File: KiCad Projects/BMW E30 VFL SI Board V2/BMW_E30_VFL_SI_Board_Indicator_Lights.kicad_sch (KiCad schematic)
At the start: 14 parts, among them J1 Conn_01x13_Pin, Q5 BC337-25, Q6 BC337-25, Q7 BC337-25

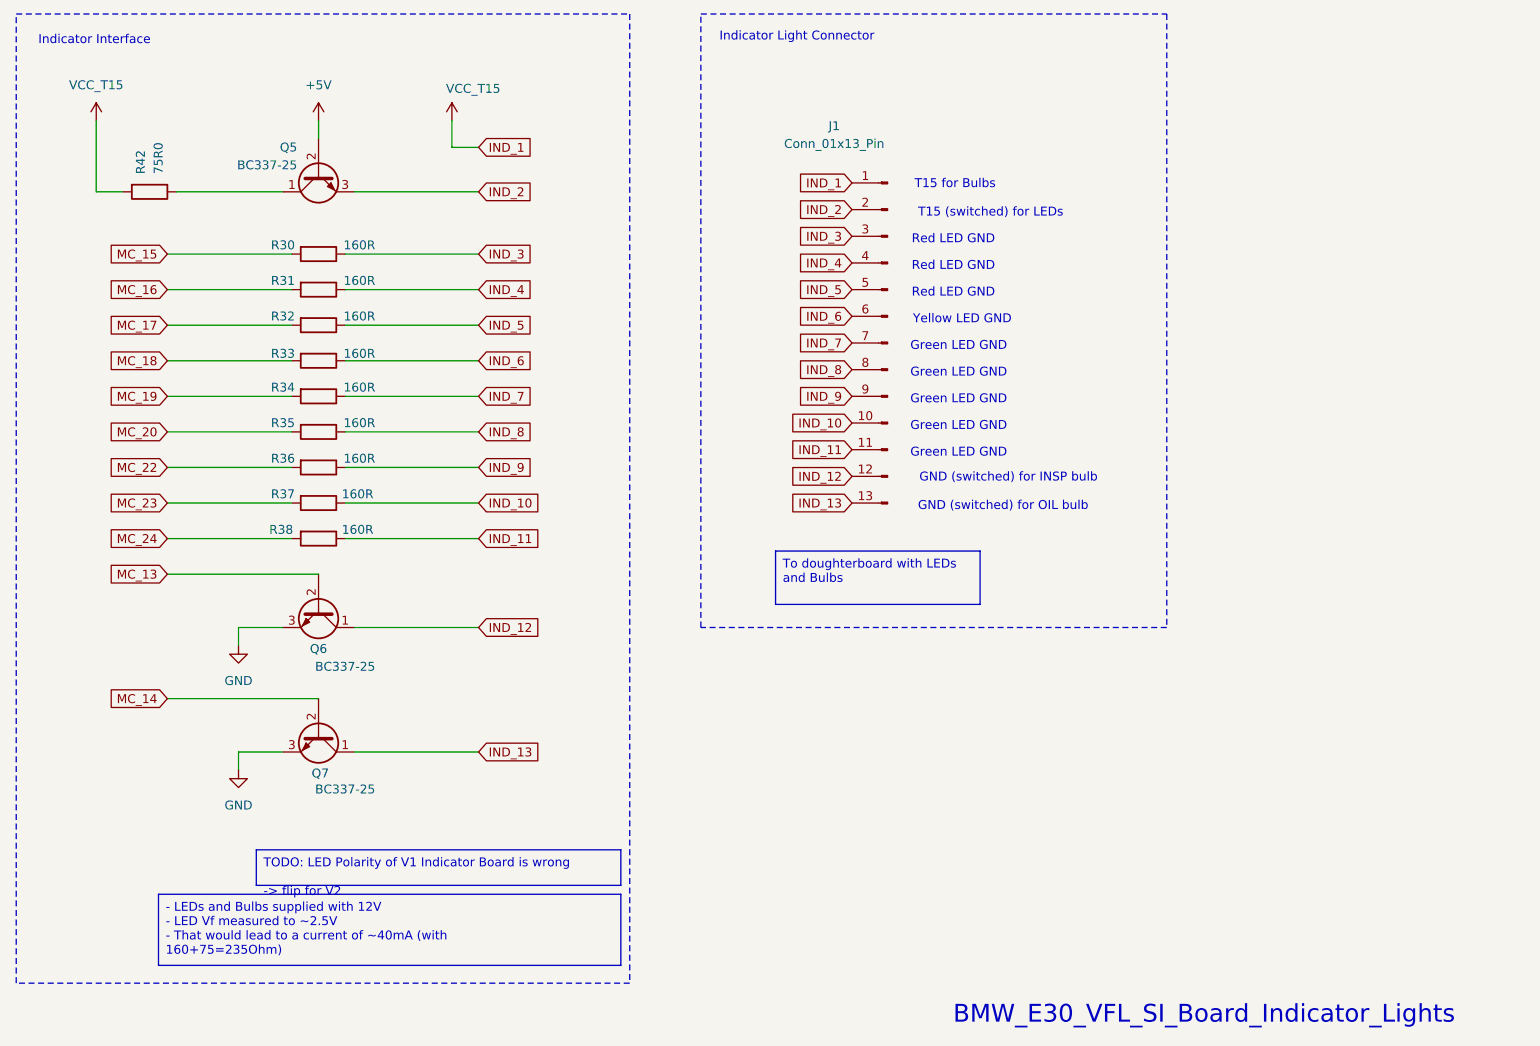
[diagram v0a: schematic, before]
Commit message: V2 Board Updates
Added in extra resistors, cap, and diode that were added to a  particular version of the SI board from the USDM on the comparator circuit. Updated the schematic diagram of the comparator circuit to improve readability. Updated the clock frequency measured with a scope. Made a few minor layout improvements including moving the "JP" connections inwards as not to interfere with the plastic housing for the PCB in the cluster and other minor layout errors such as swapped reference designators. Updated info on where the +5V regulator gets its source voltage from. These updates are reflected in schematic version V2.1 as denoted in the title box (not in the title of the schematic file).
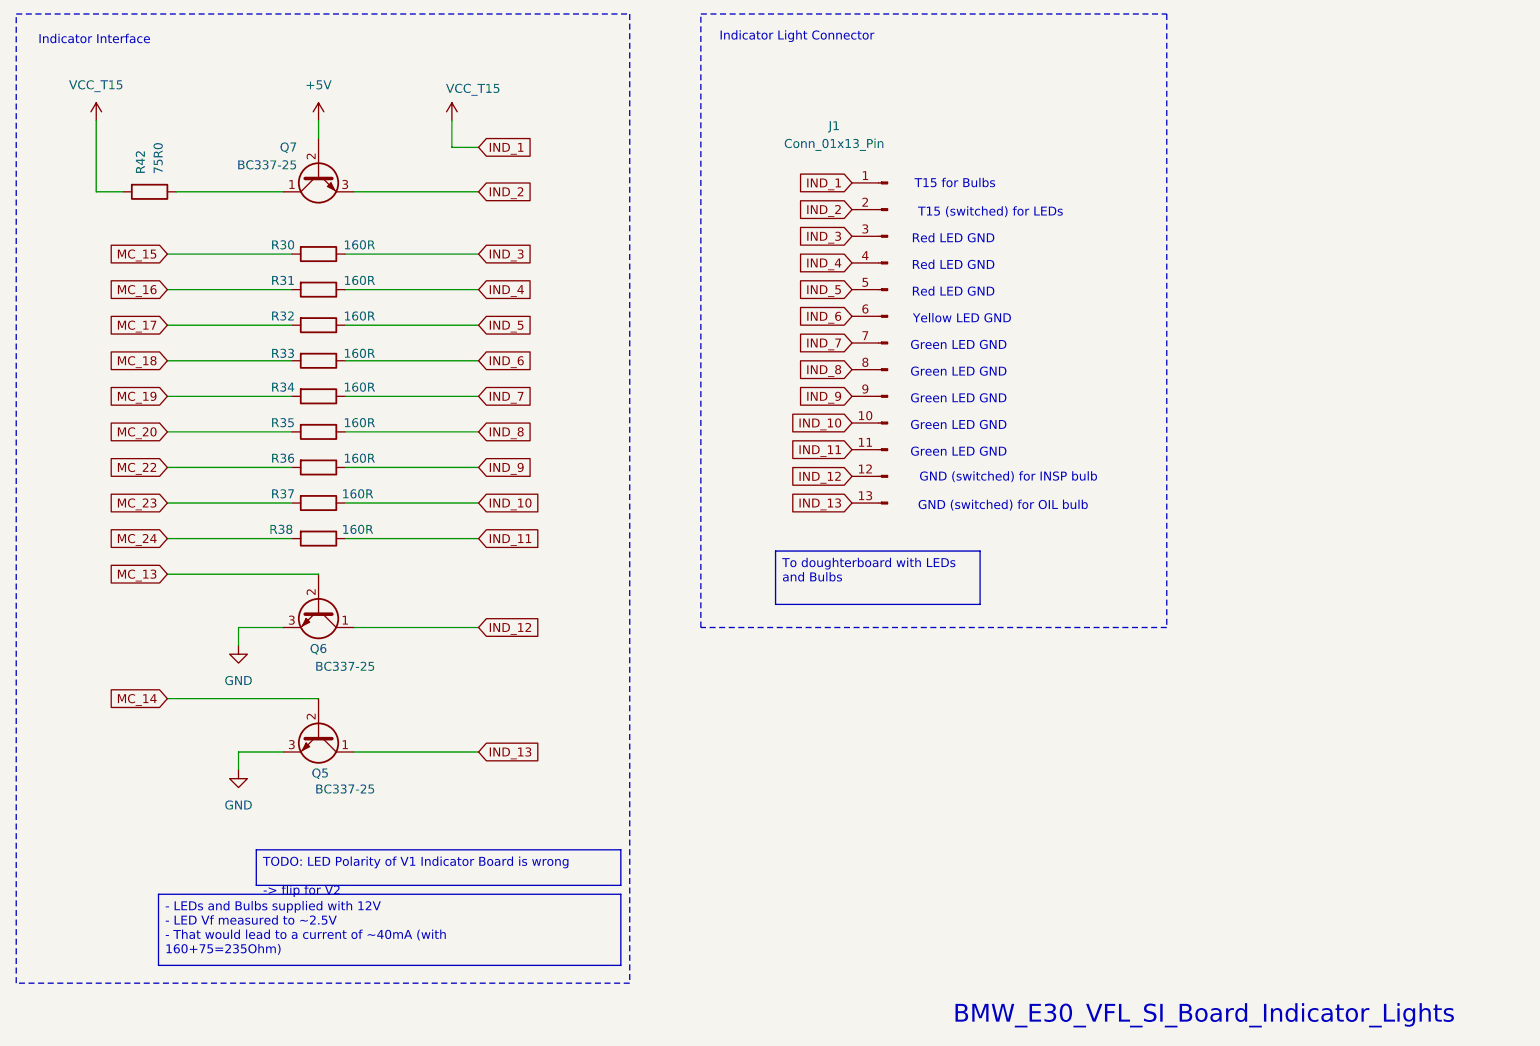
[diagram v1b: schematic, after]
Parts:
- renumbered Q7 to Q5, Q5 to Q7
